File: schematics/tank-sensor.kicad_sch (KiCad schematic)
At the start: 30 parts, among them J10 Solar Panel, J11 SDLA12TA Charge module, J12 XL6009E1 DC-DC converter, J13 BME280 3.3V, J8 Pressure Sensor, J9 Battery Connector, K1 EC2-12NU, Q1 BS170, U1 ESP32-C6-DevKitC-1, U2 TSR_1-2450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

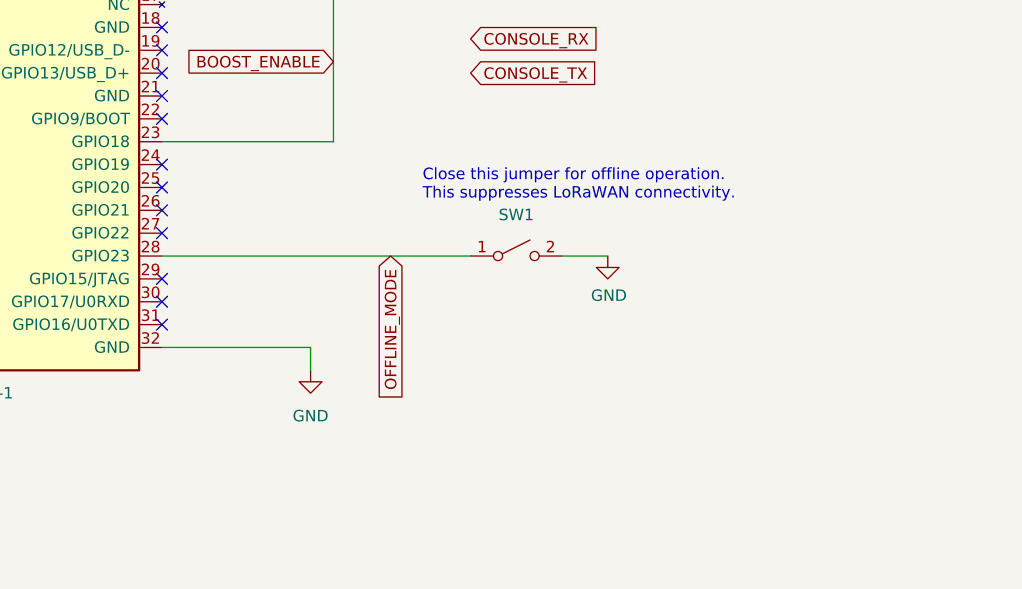
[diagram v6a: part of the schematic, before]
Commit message: Removed the on/off button
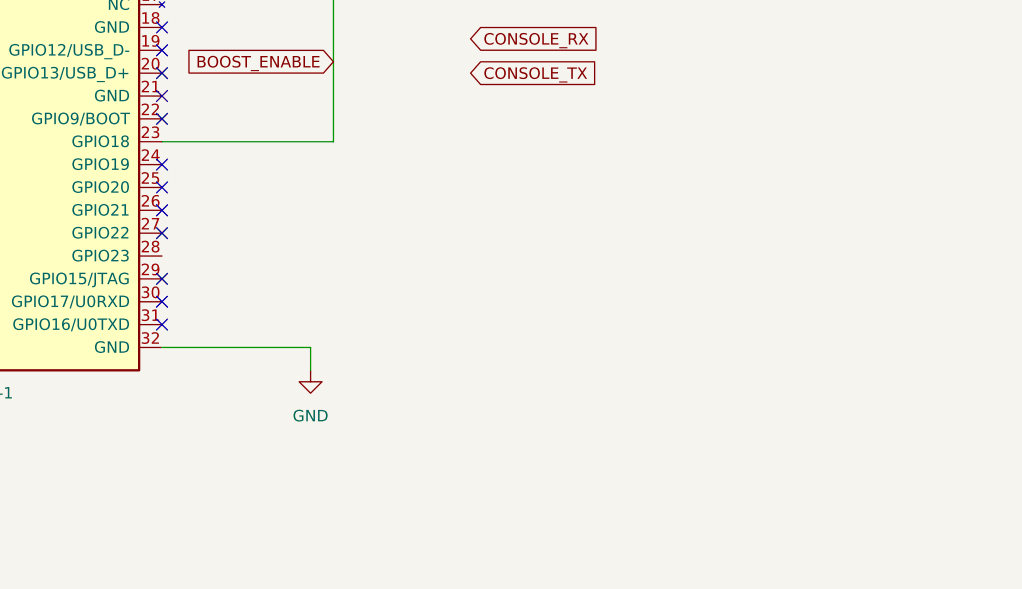
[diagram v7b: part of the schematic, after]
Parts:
- removed SW1: ~, symbol Switch:SW_SPST
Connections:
- net OFFLINE_MODE: no longer names the net of U1.28 (GPIO23)
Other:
- note removed: "Close this jumper for offline operation. This suppresses LoRaWAN connectivity."
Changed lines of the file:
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@@
 	(wire
 		(pts
-			(xy 137.16 149.86) (xy 171.45 149.86)
-		)
-		(stroke
-			(width 0)
-			(type default)
-		)
-	)
-	(wire
-		(pts
 			(xy 62.23 40.64) (xy 88.9 40.64)
 		)
@@
 	(wire
 		(pts
-			(xy 181.61 149.86) (xy 186.69 149.86)
-		)
-		(stroke
-			(width 0)
-			(type default)
-		)
-	)
-	(wire
-		(pts
 			(xy 27.94 20.32) (xy 27.94 43.18)
 		)
@@
 		)
 	)
-	(text "Close this jumper for offline operation.\nThis suppresses LoRaWAN connectivity."
-		(exclude_from_sim no)
-		(at 166.116 143.764 0)
-		(effects
-			(font
-				(size 1.27 1.27)
-			)
-			(justify left bottom)
-		)
-	)
 	(global_label "PRESS_SENSE"
 		(shape input)
@@
 		)
 	)
-	(global_label "OFFLINE_MODE"
-		(shape input)
-		(at 162.56 149.86 270)
-		(fields_autoplaced yes)
-		(effects
-			(font
-				(size 1.27 1.27)
-			)
-			(justify right)
-		)
-		(property "Intersheetrefs" "${INTERSHEET_REFS}"
-			(at 162.56 166.6338 90)
-			(effects
-				(font
-					(size 1.27 1.27)
-				)
-				(justify right)
-				(hide yes)
-			)
-		)
-	)
 	(global_label "BOOST_ENABLE"
 		(shape input)
@@
 	)
 	(symbol
-		(lib_id "Switch:SW_SPST")
-		(at 176.53 149.86 0)
-		(unit 1)
-		(exclude_from_sim no)
-		(in_bom yes)
-		(on_board yes)
-		(dnp no)
-		(property "Reference" "SW1"
-			(at 176.53 145.288 0)
-			(effects
-				(font
-					(size 1.27 1.27)
-				)
-			)
-		)
-		(property "Value" "~"
-			(at 176.53 146.2024 0)
-			(effects
-				(font
-					(size 1.27 1.27)
-				)
-			)
-		)
-		(property "Footprint" ""
-			(at 176.53 149.86 0)
-			(effects
-				(font
-					(size 1.27 1.27)
-				)
-				(hide yes)
-			)
-		)
-		(property "Datasheet" "~"
-			(at 176.53 149.86 0)
-			(effects
-				(font
-					(size 1.27 1.27)
-				)
-				(hide yes)
-			)
-		)
-		(property "Description" ""
-			(at 176.53 149.86 0)
-			(effects
-				(font
-					(size 1.27 1.27)
-				)
-				(hide yes)
-			)
-		)
-		(pin "1"
-		)
-		(pin "2"
-		)
-		(instances
-			(project "tank-sensor"
-				(path "/a113f251-aa94-483d-8b1b-4a797e2f25c2"
-					(reference "SW1")
-					(unit 1)
-				)
-			)
-		)
-	)
-	(symbol
 		(lib_id "Connector_Generic:Conn_01x01")
 		(at 252.73 115.57 180)
@@
 					(unit 1)
 				)
-			)
-		)
-	)
-	(symbol
-		(lib_id "power:GND")
-		(at 186.69 149.86 0)
-		(unit 1)
-		(exclude_from_sim no)
-		(in_bom yes)
-		(on_board yes)
-		(dnp no)
-		(property "Reference" "#PWR03"
-			(at 186.69 156.21 0)
-			(effects
-				(font
-					(size 1.27 1.27)
-				)
-				(hide yes)
-			)
-		)
-		(property "Value" "GND"
-			(at 186.817 154.2542 0)
-			(effects
-				(font
-					(size 1.27 1.27)
-				)
-			)
-		)
-		(property "Footprint" ""
-			(at 186.69 149.86 0)
-			(effects
-				(font
-					(size 1.27 1.27)
-				)
-				(hide yes)
-			)
-		)
-		(property "Datasheet" ""
-			(at 186.69 149.86 0)
-			(effects
-				(font
-					(size 1.27 1.27)
-				)
-				(hide yes)
-			)
-		)
-		(property "Description" ""
-			(at 186.69 149.86 0)
-			(effects
-				(font
-					(size 1.27 1.27)
-				)
-				(hide yes)
-			)
-		)
-		(pin "1"
-		)
-		(instances
-			(project "tank-sensor"
-				(path "/a113f251-aa94-483d-8b1b-4a797e2f25c2"
-					(reference "#PWR03")
-					(unit 1)
-				)
